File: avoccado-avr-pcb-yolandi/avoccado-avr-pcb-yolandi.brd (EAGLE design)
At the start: 50 x 50 mm, 23 parts, among them Q1 16MHz, Q2 FET, U2 MCP73831

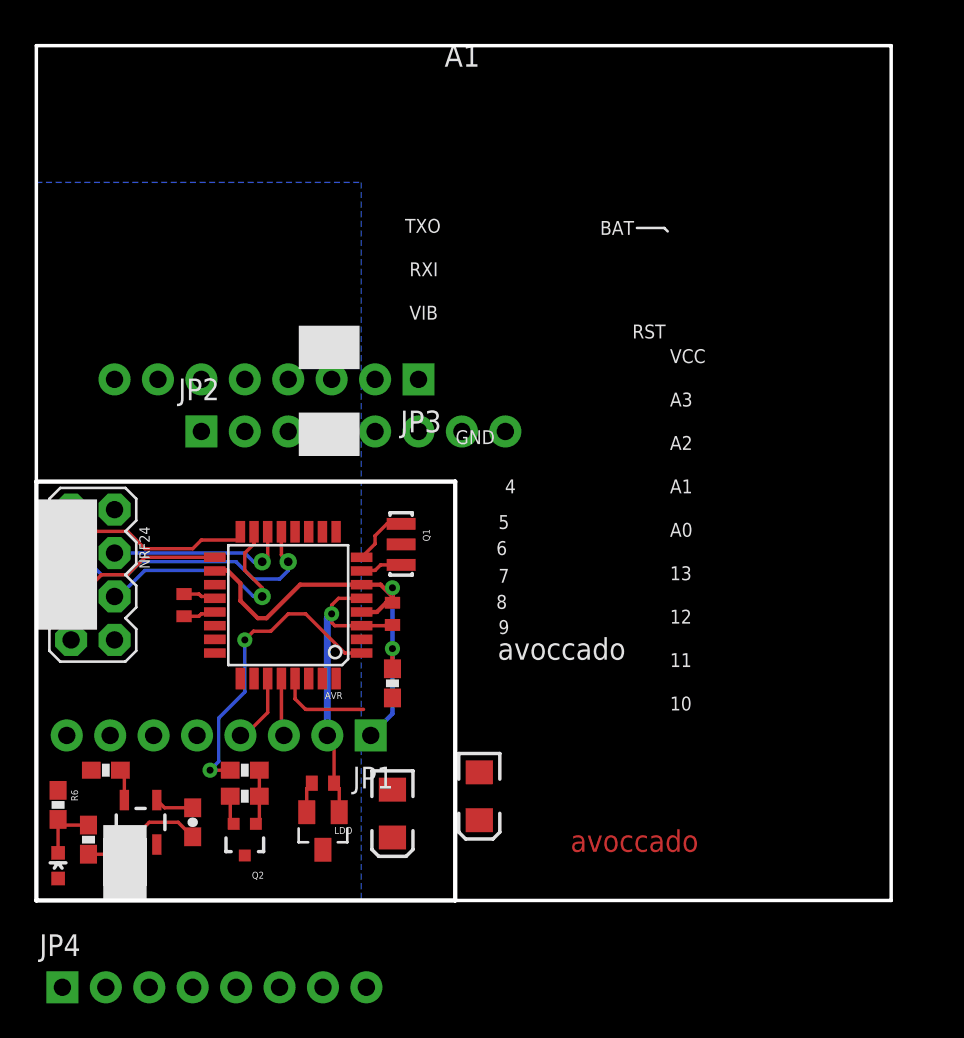
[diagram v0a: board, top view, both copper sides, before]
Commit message: routing yolandi
added DTR-reset latch circuit with 0.1uF C
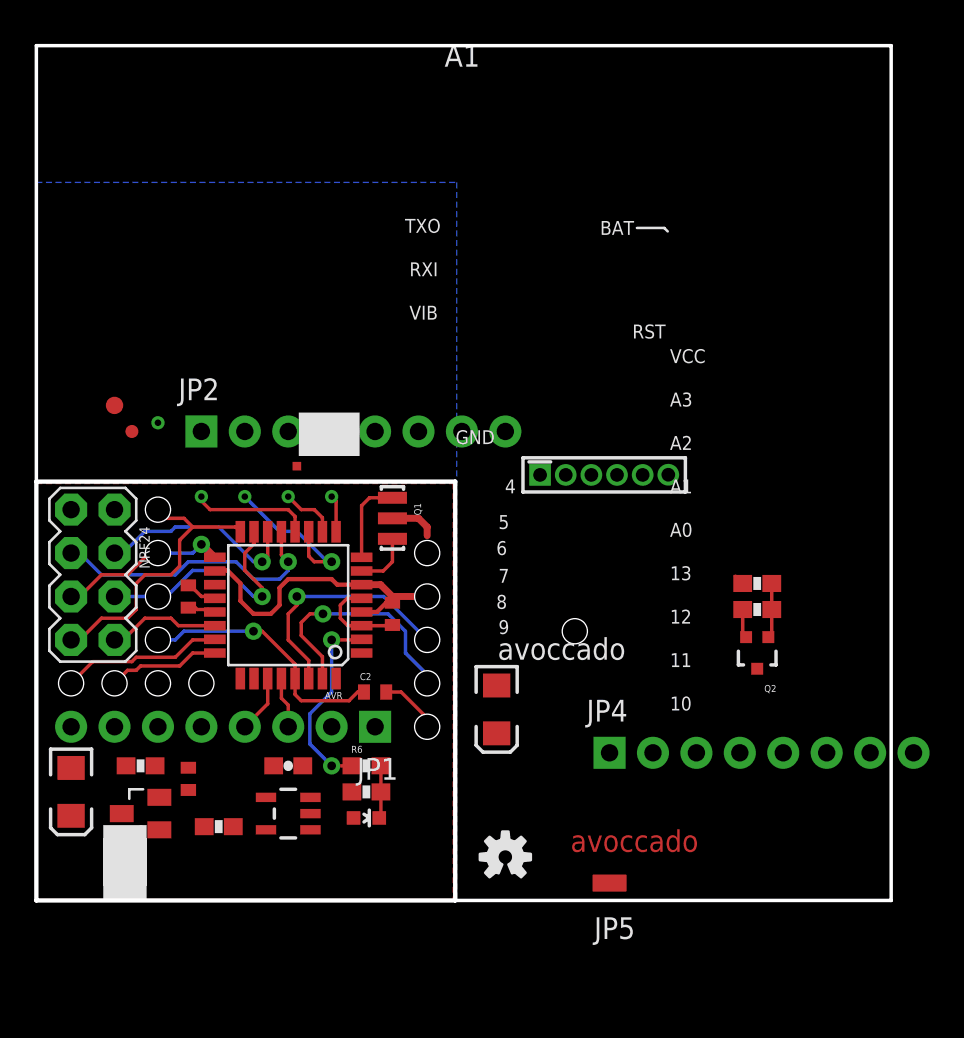
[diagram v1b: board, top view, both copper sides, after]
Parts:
- added C2: 0.1uF, SparkFun:C0402
- added JP10, JP11, JP12, JP13, JP14, JP15, JP16, JP17, JP18, JP6, JP7, JP8, JP9: M01POGOPIN_HOLE_0.58, SparkFun-Connectors:1X01_POGOPIN_HOLE_0.58
- added JP5: M01SMD, SparkFun-Connectors:LUXEON-PAD
- added LOGO1: OSHW-LOGOS, SparkFun-Aesthetics:OSHW-LOGO-S
- added TP1, TP5, TP6, TP7, TP8: TEST-POINTTP_15TH_THRU, SparkFun-Passives:TP_15TH
- added TP2: TEST-POINT3X4, SparkFun-Passives:PAD.03X.04
- added TP3: TEST-POINT3, SparkFun-Passives:PAD.03X.03
- added TP4: TEST-POINT2, SparkFun-Passives:PAD.02X.02
- added U$1: AVR_MINI_PROGSMD, SparkFun-Connectors:AVR_MINI_PROG
- JP3: value (none) -> M01POGOPIN_HOLE_0.58; device SparkFun-Connectors:1X08_PIN1_NO_SILK -> SparkFun-Connectors:1X01_POGOPIN_HOLE_0.58
- moved JP4 34.8 mm to (33.5, 8.64)
- moved Q2 31.9 mm to (42.2, 14.5)
- moved R1 31.9 mm to (42.2, 18.5)
- moved R5 31.9 mm to (42.2, 17.0)
- moved C13 23.9 mm to (2.03, 6.35)
- moved D1 18.2 mm to (19.3, 4.83), turned to 270 degrees
- moved R6 18.2 mm to (19.3, 7.87), turned to 0 degrees
- moved R4 16.5 mm to (19.3, 6.35), turned to 180 degrees
- moved R2 15.5 mm to (6.10, 7.87), turned to 0 degrees
- moved LDO 10.7 mm to (6.10, 5.08), turned to 90 degrees
- moved JP3 10.2 mm to (22.9, 20.3), turned to 0 degrees
- moved U2 8.65 mm to (14.7, 5.08), turned to 90 degrees
- moved C19 8.62 mm to (26.9, 11.2)
- moved C10 7.88 mm to (8.89, 7.11), turned to 90 degrees
- moved R3 7.38 mm to (10.7, 4.32)
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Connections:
- net BUS renamed 5V
- net N$3 renamed CHG-PROG
- net N$4 renamed SOC
- removed net N$5: R6.1
- new net DTR: C2.2, JP10.1
- net 3V3: now also JP11.1, JP16.1
- net A7: now also NRF24.8
- net D10: no longer JP3.5
- net D4: now also R6.1
- net D5: now also TP1.P$1
- net D6: now also TP6.P$1
- net D7: now also TP7.P$1; no longer JP3.1
- net D8: now also TP8.P$1; no longer JP3.3
- net D9: no longer JP3.4
- net GND: now also JP6.1
- net MISO: now also JP12.1; no longer JP3.7
- net MOSI: now also JP14.1; no longer JP3.6
- net RESET: now also C2.1, JP15.1
- net RXI: now also JP8.1
- net SCK: now also JP13.1; no longer JP3.8
- net TXO: now also JP9.1
- net VBAT: now also JP7.1
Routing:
- net D3: track 18.1 -> 1.08 mm, vias 2 -> 0
- net GND: track 26.6 -> 11.6 mm, vias 1 -> 0
- net RXI: track 0.00 -> 14.2 mm, vias 0 -> 1
- net TXO: track 0.00 -> 14.1 mm, vias 0 -> 1
- net D4: track 0.00 -> 11.4 mm, vias 0 -> 2
- net 3V3: track 28.7 -> 18.4 mm, vias 2 -> 0
- net RESET: track 5.45 -> 15.2 mm, vias 0 -> 1
- net D7: track 0.00 -> 9.56 mm, vias 0 -> 1
- net A0: track 0.00 -> 9.47 mm
- net D8: track 0.00 -> 7.01 mm
- net A1: track 0.00 -> 6.60 mm
- net A7: track 0.00 -> 6.57 mm
- net DTR: track 0.00 -> 3.54 mm
- net D6: track 0.00 -> 3.33 mm
- net SOC: track 2.33 -> 0.00 mm
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- added copper zone on layer 1, net GND

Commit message: routing yolandi, lower part with PDU
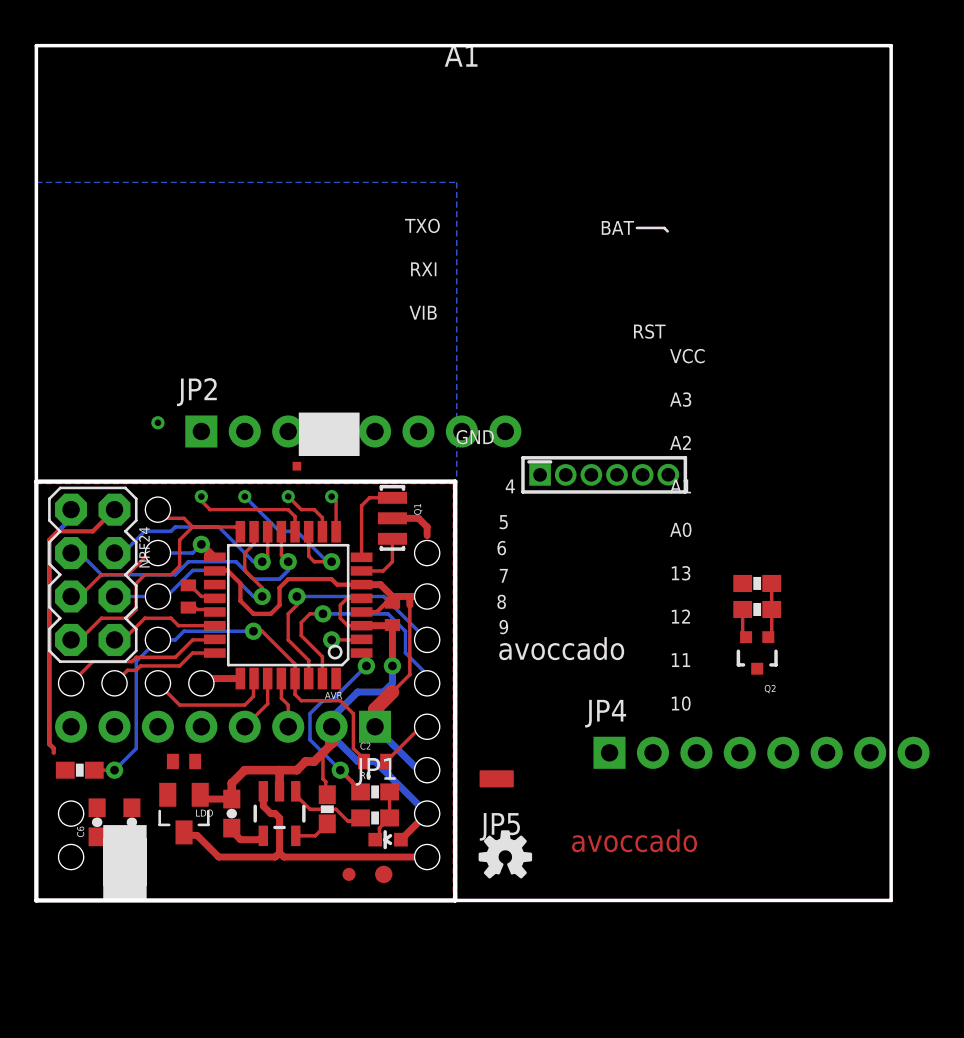
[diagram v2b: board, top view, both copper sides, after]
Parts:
- removed C13, C19: 10uF, SparkFun:EIA3216
- added C5, C6: 4.7uF, SparkFun-Capacitors:0603-CAP
- added JP19, JP20, JP21, JP22: M01POGOPIN_HOLE_0.58, SparkFun-Connectors:1X01_POGOPIN_HOLE_0.58
- moved TP2 31.6 mm to (20.3, 1.52)
- moved TP3 28.9 mm to (18.3, 1.52)
- moved JP6 19.8 mm to (22.9, 5.08)
- moved JP7 15.8 mm to (22.9, 2.54)
- moved JP17 14.2 mm to (22.9, 7.62)
- moved JP18 10.2 mm to (2.03, 2.54)
- moved JP16 9.16 mm to (2.03, 5.08)
- moved JP5 8.99 mm to (26.9, 7.11)
- moved R3 6.43 mm to (17.0, 5.33), turned to 270 degrees
- moved C4 4.33 mm to (11.4, 5.08), turned to 90 degrees
- moved C2 4.06 mm to (19.8, 8.13)
- moved R2 3.57 mm to (2.54, 7.62), turned to 180 degrees
- moved LDO 2.54 mm to (8.64, 5.08), turned to 180 degrees
- moved D1 1.80 mm to (20.6, 3.56), turned to 90 degrees
- moved R4 1.61 mm to (19.8, 4.83)
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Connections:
- net 3V3: now also C6.1; no longer C13.A
- net A0: now also JP19.1
- net A1: now also JP20.1
- net A2: now also JP21.1
- net A3: now also JP22.1
- net D3: now also R6.1; no longer R1.1
- net D4: now also R1.1; no longer R6.1
- net GND: now also C5.2, C6.2; no longer C13.C, C19.C
- net VBAT: now also C5.1; no longer C19.A
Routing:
- net GND: track 11.6 -> 60.4 mm, vias 0 -> 1
- net 3V3: track 18.4 -> 48.0 mm
- net VBAT: track 0.00 -> 19.2 mm
- net RESET: track 15.2 -> 27.6 mm, vias 1 -> 2
- net D3: track 1.08 -> 11.6 mm, vias 0 -> 2
- net D4: track 11.4 -> 1.77 mm, vias 2 -> 1
- net A3: track 0.00 -> 7.38 mm
- net SOC: track 0.00 -> 4.67 mm
- net A2: track 0.00 -> 2.40 mm
- net 5V: track 0.00 -> 2.31 mm
- net CHG-PROG: track 0.00 -> 2.14 mm

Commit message: routing the buffered load output
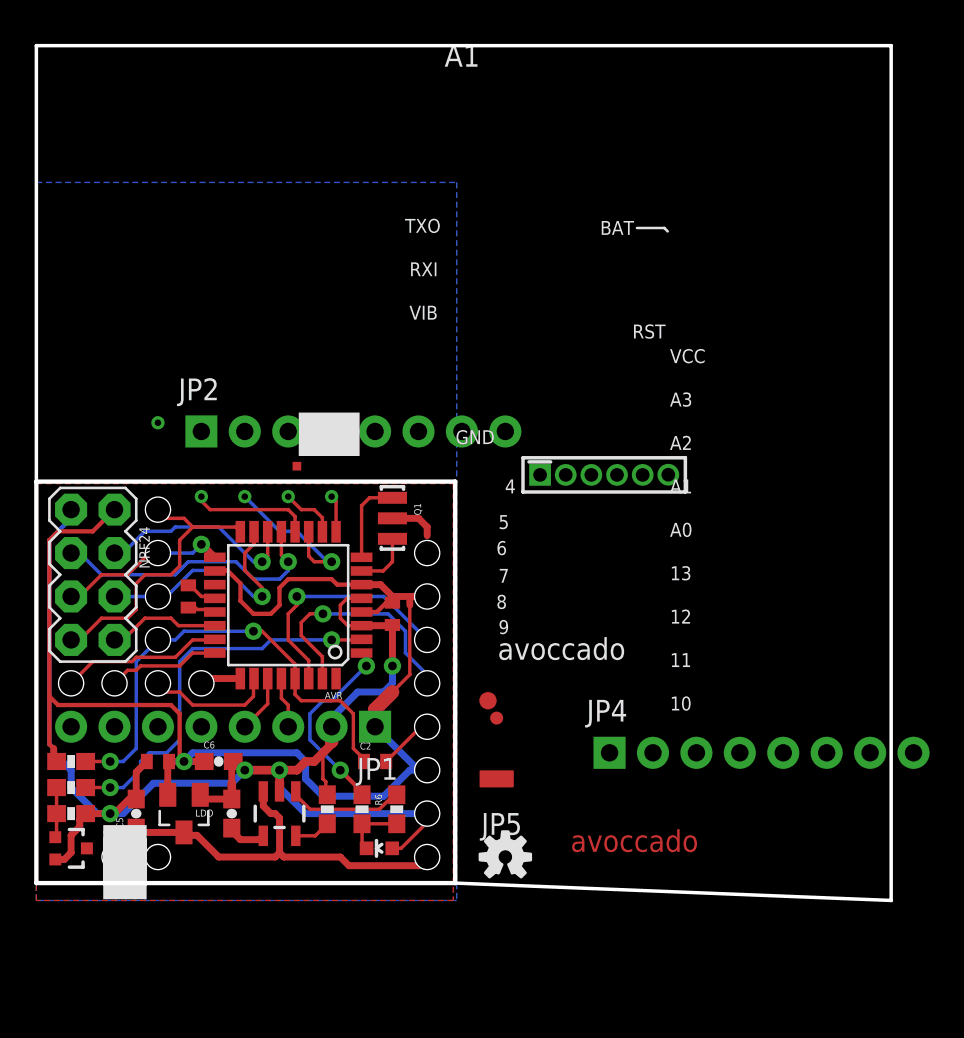
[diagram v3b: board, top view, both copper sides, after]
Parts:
- moved R1 41.9 mm to (2.03, 6.60), turned to 180 degrees
- moved R5 41.9 mm to (2.03, 5.08), turned to 180 degrees
- moved Q2 41.7 mm to (2.03, 3.05), turned to 270 degrees
- moved JP18 21.4 mm to (22.9, 7.62)
- moved JP17 16.5 mm to (7.11, 2.54)
- moved TP3 12.6 mm to (26.9, 10.7)
- moved TP2 11.8 mm to (26.4, 11.7)
- moved C6 7.95 mm to (10.7, 8.13), turned to 0 degrees
- moved JP16 3.59 mm to (4.57, 2.54)
- moved C10 1.52 mm to (7.11, 8.13), turned to 180 degrees
- moved R4 1.37 mm to (21.1, 5.33), turned to 90 degrees
- moved R6 1.27 mm to (19.1, 5.33), turned to 270 degrees
- moved D1 0.72 mm to (20.1, 3.05)
- moved R2 0.72 mm to (2.03, 8.13)
- moved C5 0.57 mm to (5.84, 5.08)
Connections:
- net 3V3: now also JP18.1
- net 5V: now also JP17.1
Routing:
- net 3V3: track 48.0 -> 80.7 mm, vias 0 -> 1
- net GND: track 60.4 -> 89.7 mm, vias 1 -> 4
- net D4: track 1.77 -> 22.7 mm, vias 1 -> 2
- net VBAT: track 19.2 -> 22.5 mm
- net SOC: track 4.67 -> 6.82 mm
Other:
- outline, holes or cut-outs redrawn

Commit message: wip yolandi
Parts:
- added JP24: M01POGOPIN_HOLE_0.58, SparkFun-Connectors:1X01_POGOPIN_HOLE_0.58
- moved JP17 15.7 mm to (22.9, 2.54)
- moved JP7 13.2 mm to (9.65, 2.54)
- moved JP16 12.7 mm to (17.3, 2.54)
- moved C4 0.25 mm to (11.4, 5.33)
- moved C5 0.25 mm to (5.84, 5.33)
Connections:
- net GND: now also JP3.1
- net VBAT: now also JP24.1
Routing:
- net GND: track 89.7 -> 119.4 mm, vias 4 -> 5
- net 5V: track 2.31 -> 14.7 mm, vias 0 -> 1
- net VBAT: track 22.5 -> 14.1 mm
- net D4: track 22.7 -> 20.9 mm
- net RESET: track 27.9 -> 29.2 mm
- net RXI: track 14.2 -> 13.0 mm
- net TXO: track 14.1 -> 13.0 mm

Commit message: wip add silkscreen
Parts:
- removed JP2: (no value), SparkFun-Connectors:1X08_PIN1_NO_SILK
- added JP23, JP25, JP26: M01POGOPIN_HOLE_0.58, SparkFun-Connectors:1X01_POGOPIN_HOLE_0.58
- moved JP7 26.3 mm to (31.5, 17.3)
- moved JP16 18.8 mm to (29.0, 17.3)
- moved JP17 5.08 mm to (17.8, 2.54)
- moved D1 2.81 mm to (22.9, 2.79), turned to 0 degrees
- moved Q1 0.76 mm to (20.8, 23.1), turned to 0 degrees
- moved TP4 0.51 mm to (15.2, 25.9)
- moved JP24 0.51 mm to (7.62, 2.54)
- moved LDO 0.36 mm to (8.89, 5.33)
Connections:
- net GND: now also D1.C, JP25.1, JP26.1; no longer D1.A
- net LED: now also D1.A; no longer D1.C
- net VIBR: now also JP23.1
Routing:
- net GND: track 119.4 -> 125.6 mm, vias 5 -> 6
- net 5V: track 14.7 -> 8.95 mm
- net VBAT: track 14.1 -> 19.0 mm, vias 0 -> 1
- net N$2: track 3.37 -> 5.83 mm
- net VIBR: track 0.00 -> 2.33 mm
- net CHG-PROG: track 2.14 -> 4.33 mm
- net LED: track 3.58 -> 5.66 mm
- net 3V3: track 80.7 -> 79.5 mm
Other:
- board text added: "3V"
- board text added: "ATMEGA328"
- board text added: "AVOCCADO YOLANDI V1"
- board text added: "DT"
- board text added: "GROUND"
- board text added: "RX"
- board text added: "TX"
- board text added: "Vb"
- board text added: "Vcc"
- board text added: "Vin"
- board text removed: "10"
- board text removed: "GND"
- board text removed: "RXI"
- board text removed: "TXO"
- board text removed: "VCC"
